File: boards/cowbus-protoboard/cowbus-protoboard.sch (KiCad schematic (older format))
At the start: 2 parts, among them P1 CPU_TO_PERIPH, P2 PERIPH_TO_MCU

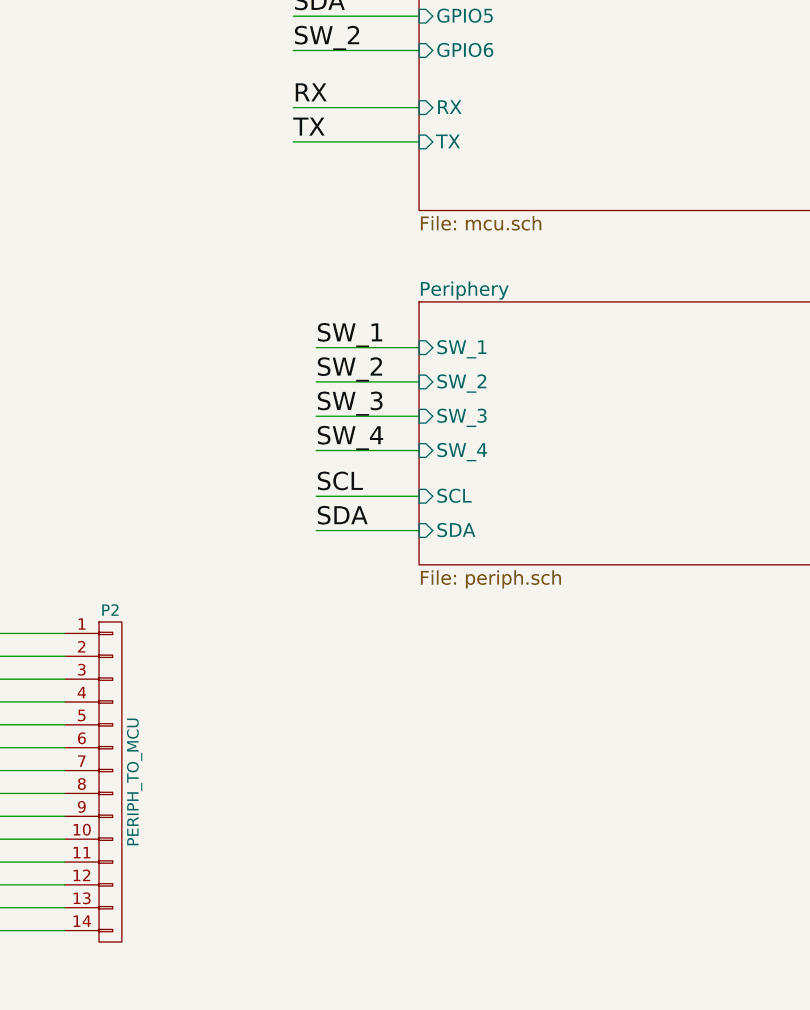
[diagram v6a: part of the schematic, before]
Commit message: added GPIO18, better 3V3, better GND
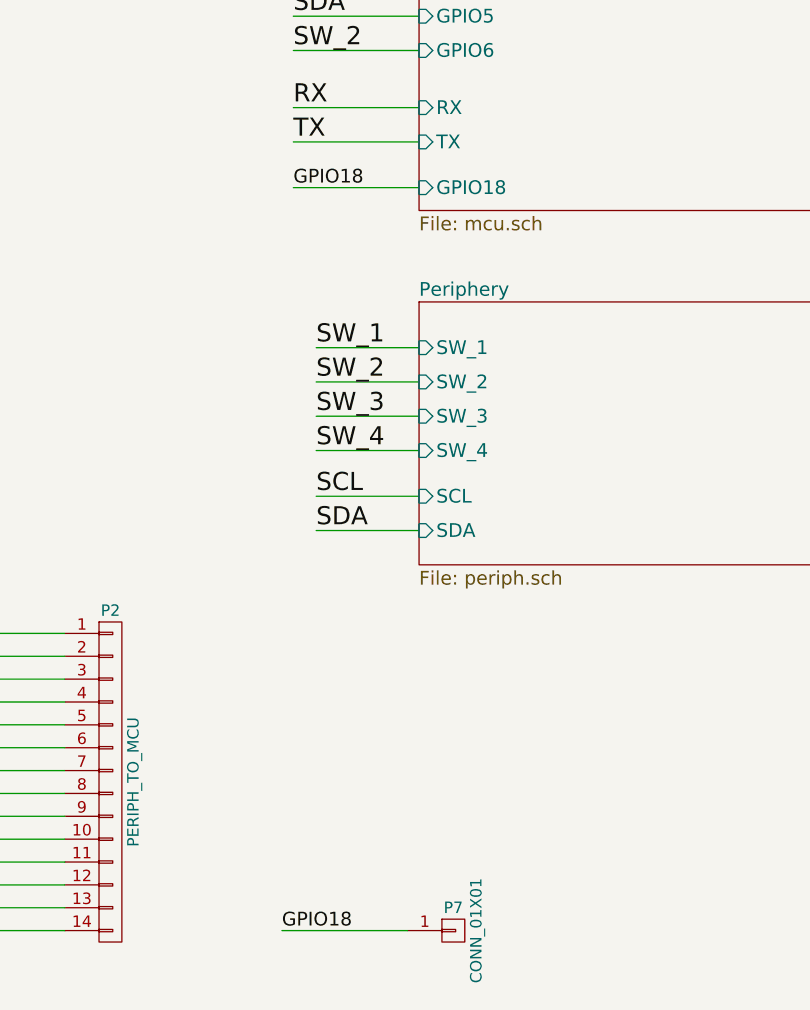
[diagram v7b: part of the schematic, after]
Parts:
- added P7: CONN_01X01, Pin_Headers:Pin_Header_Straight_1x01, symbol CONN_01X01
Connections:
- new net GPIO18: P7.1 (P1)
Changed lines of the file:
@@
 F22 "TX" I L 5150 3700 60
 F23 "RX" I L 5150 3550 60
+F24 "GPIO18" I L 5150 3900 60
 $EndSheet
 $Sheet
@@
 F2 "VCC_OUT" I L 1450 2200 60
 $EndSheet
-Wire Wire Line
-	8200 4600 8800 4600
-Wire Wire Line
-	8200 4750 8800 4750
-Wire Wire Line
-	8200 4900 8800 4900
 Text Label 8800 4600 2    79   ~ 0
 LED_R
@@
 Text Label 8800 4900 2    79   ~ 0
 LED_B
-Wire Wire Line
-	8200 2700 8800 2700
-Wire Wire Line
-	8200 2850 8800 2850
-Wire Wire Line
-	8200 3000 8800 3000
 Text Label 8800 2700 2    79   ~ 0
 LED_R
@@
 LED_B
 $Comp
-L VCC #PWR1
+L VCC #PWR01
 U 1 1 55A6ED40
 P 1150 1300
-F 0 "#PWR1" H 1150 1150 50  0001 C CNN
+F 0 "#PWR01" H 1150 1150 50  0001 C CNN
 F 1 "VCC" H 1150 1450 50  0000 C CNN
 F 2 "" H 1150 1300 60  0000 C CNN
@@
 $EndComp
 $Comp
-L VCC #PWR2
+L VCC #PWR02
 U 1 1 55A73D74
 P 4900 1300
-F 0 "#PWR2" H 4900 1150 50  0001 C CNN
+F 0 "#PWR02" H 4900 1150 50  0001 C CNN
 F 1 "VCC" H 4900 1450 50  0000 C CNN
 F 2 "" H 4900 1300 60  0000 C CNN
@@
 $EndComp
 $Comp
-L +3V3 #PWR3
+L +3V3 #PWR03
 U 1 1 55A75A13
 P 8550 1700
-F 0 "#PWR3" H 8550 1550 50  0001 C CNN
+F 0 "#PWR03" H 8550 1550 50  0001 C CNN
 F 1 "+3V3" H 8550 1840 50  0000 C CNN
 F 2 "" H 8550 1700 60  0000 C CNN
@@
 	1    0    0    -1
 $EndComp
-Wire Wire Line
-	8200 2200 8550 2200
-Wire Wire Line
-	8550 2200 8550 1700
-Wire Wire Line
-	1450 2200 1150 2200
-Wire Wire Line
-	1150 2200 1150 1300
-Wire Wire Line
-	5150 2200 4900 2200
-Wire Wire Line
-	4900 2200 4900 1300
-Wire Wire Line
-	8200 3150 8800 3150
 Text Label 8800 3150 2    79   ~ 0
 SW_4
-Wire Wire Line
-	5150 4600 4700 4600
-Wire Wire Line
-	5150 4750 4700 4750
-Wire Wire Line
-	5150 4900 4700 4900
-Wire Wire Line
-	5150 5050 4700 5050
 Text Label 4700 5050 0    79   ~ 0
 SW_4
-Wire Wire Line
-	5150 2400 4600 2400
-Wire Wire Line
-	5150 2550 4600 2550
-Wire Wire Line
-	5150 2700 4600 2700
-Wire Wire Line
-	5150 2850 4600 2850
-Wire Wire Line
-	5150 3000 4600 3000
-Wire Wire Line
-	5150 3150 4600 3150
-Wire Wire Line
-	5150 3300 4600 3300
-Wire Wire Line
-	8200 2400 8800 2400
-Wire Wire Line
-	8200 2550 8800 2550
 Text Label 8800 2400 2    79   ~ 0
 SW_3
@@
 Text Label 4600 2400 0    79   ~ 0
 SW_1
-Wire Wire Line
-	8200 3300 8800 3300
-Wire Wire Line
-	8200 3450 8800 3450
-Wire Wire Line
-	8200 3600 8800 3600
-Wire Wire Line
-	8200 3750 8800 3750
-Wire Wire Line
-	8200 3900 8800 3900
-Wire Wire Line
-	8200 5100 8800 5100
 Text Label 8800 5100 2    79   ~ 0
 BUZ
 Text Label 8800 3900 2    79   ~ 0
 BUZ
-Wire Wire Line
-	1900 5050 1200 5050
-Wire Wire Line
-	1900 5150 1200 5150
-Wire Wire Line
-	1900 5250 1200 5250
-Wire Wire Line
-	1900 5350 1200 5350
-Wire Wire Line
-	1900 5450 1200 5450
-Wire Wire Line
-	1900 5550 1200 5550
 Text Label 4600 3000 0    79   ~ 0
 SCL
 Text Label 4600 3150 0    79   ~ 0
 SDA
-Wire Wire Line
-	5150 5250 4700 5250
-Wire Wire Line
-	5150 5400 4700 5400
 Text Label 4700 5250 0    79   ~ 0
 SCL
@@
 	1    0    0    -1
 $EndComp
-Wire Wire Line
-	3600 5850 2900 5850
-Wire Wire Line
-	3600 5950 2900 5950
-Wire Wire Line
-	3600 6050 2900 6050
-Wire Wire Line
-	3600 6150 2900 6150
-Wire Wire Line
-	3600 6250 2900 6250
-Wire Wire Line
-	3600 6350 2900 6350
-Wire Wire Line
-	3600 6750 2900 6750
-Wire Wire Line
-	3600 6850 2900 6850
-Wire Wire Line
-	3600 6450 2900 6450
-Wire Wire Line
-	3600 6550 2900 6550
-Wire Wire Line
-	3600 6650 2900 6650
-Wire Wire Line
-	3600 6950 2900 6950
-Wire Wire Line
-	3600 7050 2900 7050
-Wire Wire Line
-	3600 7150 2900 7150
 Text Label 2900 5850 0    47   ~ 0
 GND
@@
 Text Label 2900 6950 0    47   ~ 0
 BUZ
-Wire Wire Line
-	1900 5850 1200 5850
-Wire Wire Line
-	1900 5950 1200 5950
-Wire Wire Line
-	1900 6050 1200 6050
-Wire Wire Line
-	1900 6150 1200 6150
-Wire Wire Line
-	1900 6250 1200 6250
-Wire Wire Line
-	1900 6350 1200 6350
-Wire Wire Line
-	1900 6750 1200 6750
-Wire Wire Line
-	1900 6850 1200 6850
-Wire Wire Line
-	1900 6450 1200 6450
-Wire Wire Line
-	1900 6550 1200 6550
-Wire Wire Line
-	1900 6650 1200 6650
-Wire Wire Line
-	1900 6950 1200 6950
-Wire Wire Line
-	1900 7050 1200 7050
-Wire Wire Line
-	1900 7150 1200 7150
 Text Label 1200 5850 0    47   ~ 0
 GND
@@
 	1    0    0    -1
 $EndComp
-Wire Wire Line
-	1900 5650 1200 5650
-Wire Wire Line
-	1900 5750 1200 5750
 Text Label 1200 5650 0    47   ~ 0
 GPIO15
@@
 F13 "TX" I R 8200 5450 60
 $EndSheet
-Wire Wire Line
-	5150 3550 4600 3550
-Wire Wire Line
-	5150 3700 4600 3700
 Text Label 4600 3700 0    79   ~ 0
 TX
 Text Label 4600 3550 0    79   ~ 0
 RX
-Wire Wire Line
-	8200 5300 8800 5300
-Wire Wire Line
-	8200 5450 8800 5450
 Text Label 8800 5300 2    79   ~ 0
 RX
@@
 TX
 $Comp
-L +3V3 #PWR4
+L +3V3 #PWR04
 U 1 1 55BE898C
 P 9300 1700
-F 0 "#PWR4" H 9300 1550 50  0001 C CNN
+F 0 "#PWR04" H 9300 1550 50  0001 C CNN
 F 1 "+3V3" H 9300 1840 50  0000 C CNN
 F 2 "" H 9300 1700 60  0000 C CNN
@@
 	-1   0    0    -1
 $EndComp
-Wire Wire Line
-	9650 2200 9300 2200
-Wire Wire Line
-	9300 2200 9300 1700
 Text Label 9650 2200 2    60   ~ 0
 3V3
+$Comp
+L CONN_01X01 P7
+U 1 1 55BD6FBA
+P 5300 7150
+F 0 "P7" H 5300 7250 50  0000 C CNN
+F 1 "CONN_01X01" V 5400 7150 50  0000 C CNN
+F 2 "Pin_Headers:Pin_Header_Straight_1x01" H 5300 7150 60  0001 C CNN
+F 3 "" H 5300 7150 60  0000 C CNN
+	1    5300 7150
+	1    0    0    -1
+$EndComp
+Text Label 4550 7150 0    60   ~ 0
+GPIO18
+Wire Wire Line
+	8200 4600 8800 4600
+Wire Wire Line
+	8200 4750 8800 4750
+Wire Wire Line
+	8200 4900 8800 4900
+Wire Wire Line
+	8200 2700 8800 2700
+Wire Wire Line
+	8200 2850 8800 2850
+Wire Wire Line
+	8200 3000 8800 3000
+Wire Wire Line
+	8200 2200 8550 2200
+Wire Wire Line
+	8550 2200 8550 1700
+Wire Wire Line
+	1450 2200 1150 2200
+Wire Wire Line
+	1150 2200 1150 1300
+Wire Wire Line
+	5150 2200 4900 2200
+Wire Wire Line
+	4900 2200 4900 1300
+Wire Wire Line
+	8200 3150 8800 3150
+Wire Wire Line
+	5150 4600 4700 4600
+Wire Wire Line
+	5150 4750 4700 4750
+Wire Wire Line
+	5150 4900 4700 4900
+Wire Wire Line
+	5150 5050 4700 5050
+Wire Wire Line
+	5150 2400 4600 2400
+Wire Wire Line
+	5150 2550 4600 2550
+Wire Wire Line
+	5150 2700 4600 2700
+Wire Wire Line
+	5150 2850 4600 2850
+Wire Wire Line
+	5150 3000 4600 3000
+Wire Wire Line
+	5150 3150 4600 3150
+Wire Wire Line
+	5150 3300 4600 3300
+Wire Wire Line
+	8200 2400 8800 2400
+Wire Wire Line
+	8200 2550 8800 2550
+Wire Wire Line
+	8200 3300 8800 3300
+Wire Wire Line
+	8200 3450 8800 3450
+Wire Wire Line
+	8200 3600 8800 3600
+Wire Wire Line
+	8200 3750 8800 3750
+Wire Wire Line
+	8200 3900 8800 3900
+Wire Wire Line
+	8200 5100 8800 5100
+Wire Wire Line
+	1900 5050 1200 5050
+Wire Wire Line
+	1900 5150 1200 5150
+Wire Wire Line
+	1900 5250 1200 5250
+Wire Wire Line
+	1900 5350 1200 5350
+Wire Wire Line
+	1900 5450 1200 5450
+Wire Wire Line
+	1900 5550 1200 5550
+Wire Wire Line
+	5150 5250 4700 5250
+Wire Wire Line
+	5150 5400 4700 5400
+Wire Wire Line
+	3600 5850 2900 5850
+Wire Wire Line
+	3600 5950 2900 5950
+Wire Wire Line
+	3600 6050 2900 6050
+Wire Wire Line
+	3600 6150 2900 6150
+Wire Wire Line
+	3600 6250 2900 6250
+Wire Wire Line
+	3600 6350 2900 6350
+Wire Wire Line
+	3600 6750 2900 6750
+Wire Wire Line
+	3600 6850 2900 6850
+Wire Wire Line
+	3600 6450 2900 6450
+Wire Wire Line
+	3600 6550 2900 6550
+Wire Wire Line
+	3600 6650 2900 6650
+Wire Wire Line
+	3600 6950 2900 6950
+Wire Wire Line
+	3600 7050 2900 7050
+Wire Wire Line
+	3600 7150 2900 7150
+Wire Wire Line
+	1900 5850 1200 5850
+Wire Wire Line
+	1900 5950 1200 5950
+Wire Wire Line
+	1900 6050 1200 6050
+Wire Wire Line
+	1900 6150 1200 6150
+Wire Wire Line
+	1900 6250 1200 6250
+Wire Wire Line
+	1900 6350 1200 6350
+Wire Wire Line
+	1900 6750 1200 6750
+Wire Wire Line
+	1900 6850 1200 6850
+Wire Wire Line
+	1900 6450 1200 6450
+Wire Wire Line
+	1900 6550 1200 6550
+Wire Wire Line
+	1900 6650 1200 6650
+Wire Wire Line
+	1900 6950 1200 6950
+Wire Wire Line
+	1900 7050 1200 7050
+Wire Wire Line
+	1900 7150 1200 7150
+Wire Wire Line
+	1900 5650 1200 5650
+Wire Wire Line
+	1900 5750 1200 5750
+Wire Wire Line
+	5150 3550 4600 3550
+Wire Wire Line
+	5150 3700 4600 3700
+Wire Wire Line
+	8200 5300 8800 5300
+Wire Wire Line
+	8200 5450 8800 5450
+Wire Wire Line
+	9650 2200 9300 2200
+Wire Wire Line
+	9300 2200 9300 1700
+Wire Wire Line
+	5100 7150 4550 7150
+Wire Wire Line
+	5150 3900 4600 3900
+Text Label 4600 3900 0    60   ~ 0
+GPIO18
 $EndSCHEMATC
